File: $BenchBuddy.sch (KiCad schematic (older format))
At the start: 0 parts

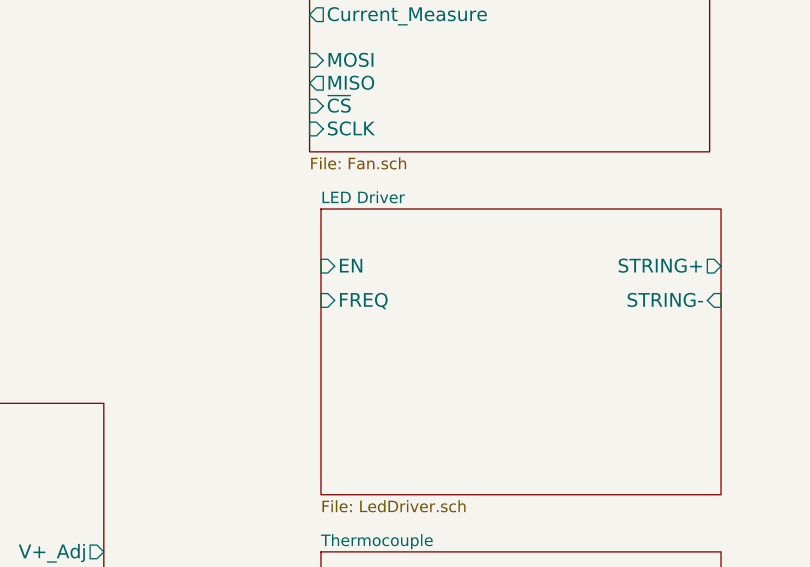
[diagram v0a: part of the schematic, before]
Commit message: Added LED Driver
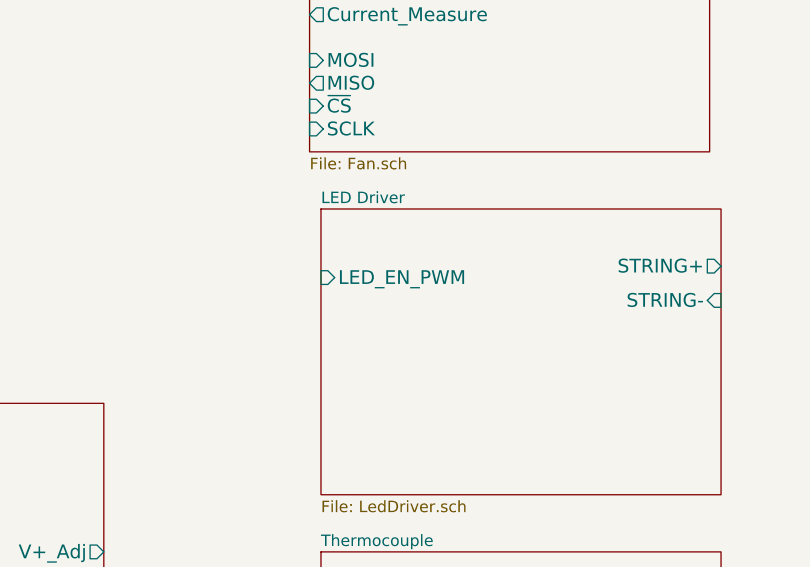
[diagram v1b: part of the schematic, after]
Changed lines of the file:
@@
-$EndSheet
-$Sheet
-S 7650 2100 1750 1250
-U 52326EDF
-F0 "LED Driver" 50
-F1 "LedDriver.sch" 50
-F2 "EN" I L 7650 2350 60
-F3 "FREQ" I L 7650 2500 60
-F4 "STRING+" O R 9400 2350 60
-F5 "STRING-" I R 9400 2500 60
 $EndSheet
 $Sheet
@@
 F9 "V-_Adj" O R 6700 3800 60
 $EndSheet
+$Sheet
+S 7650 2100 1750 1250
+U 52326EDF
+F0 "LED Driver" 50
+F1 "LedDriver.sch" 50
+F2 "STRING+" O R 9400 2350 60
+F3 "STRING-" I R 9400 2500 60
+F4 "LED_EN_PWM" I L 7650 2400 60
+$EndSheet
 $EndSCHEMATC
